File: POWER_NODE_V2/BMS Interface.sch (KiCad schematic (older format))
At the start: 11 parts

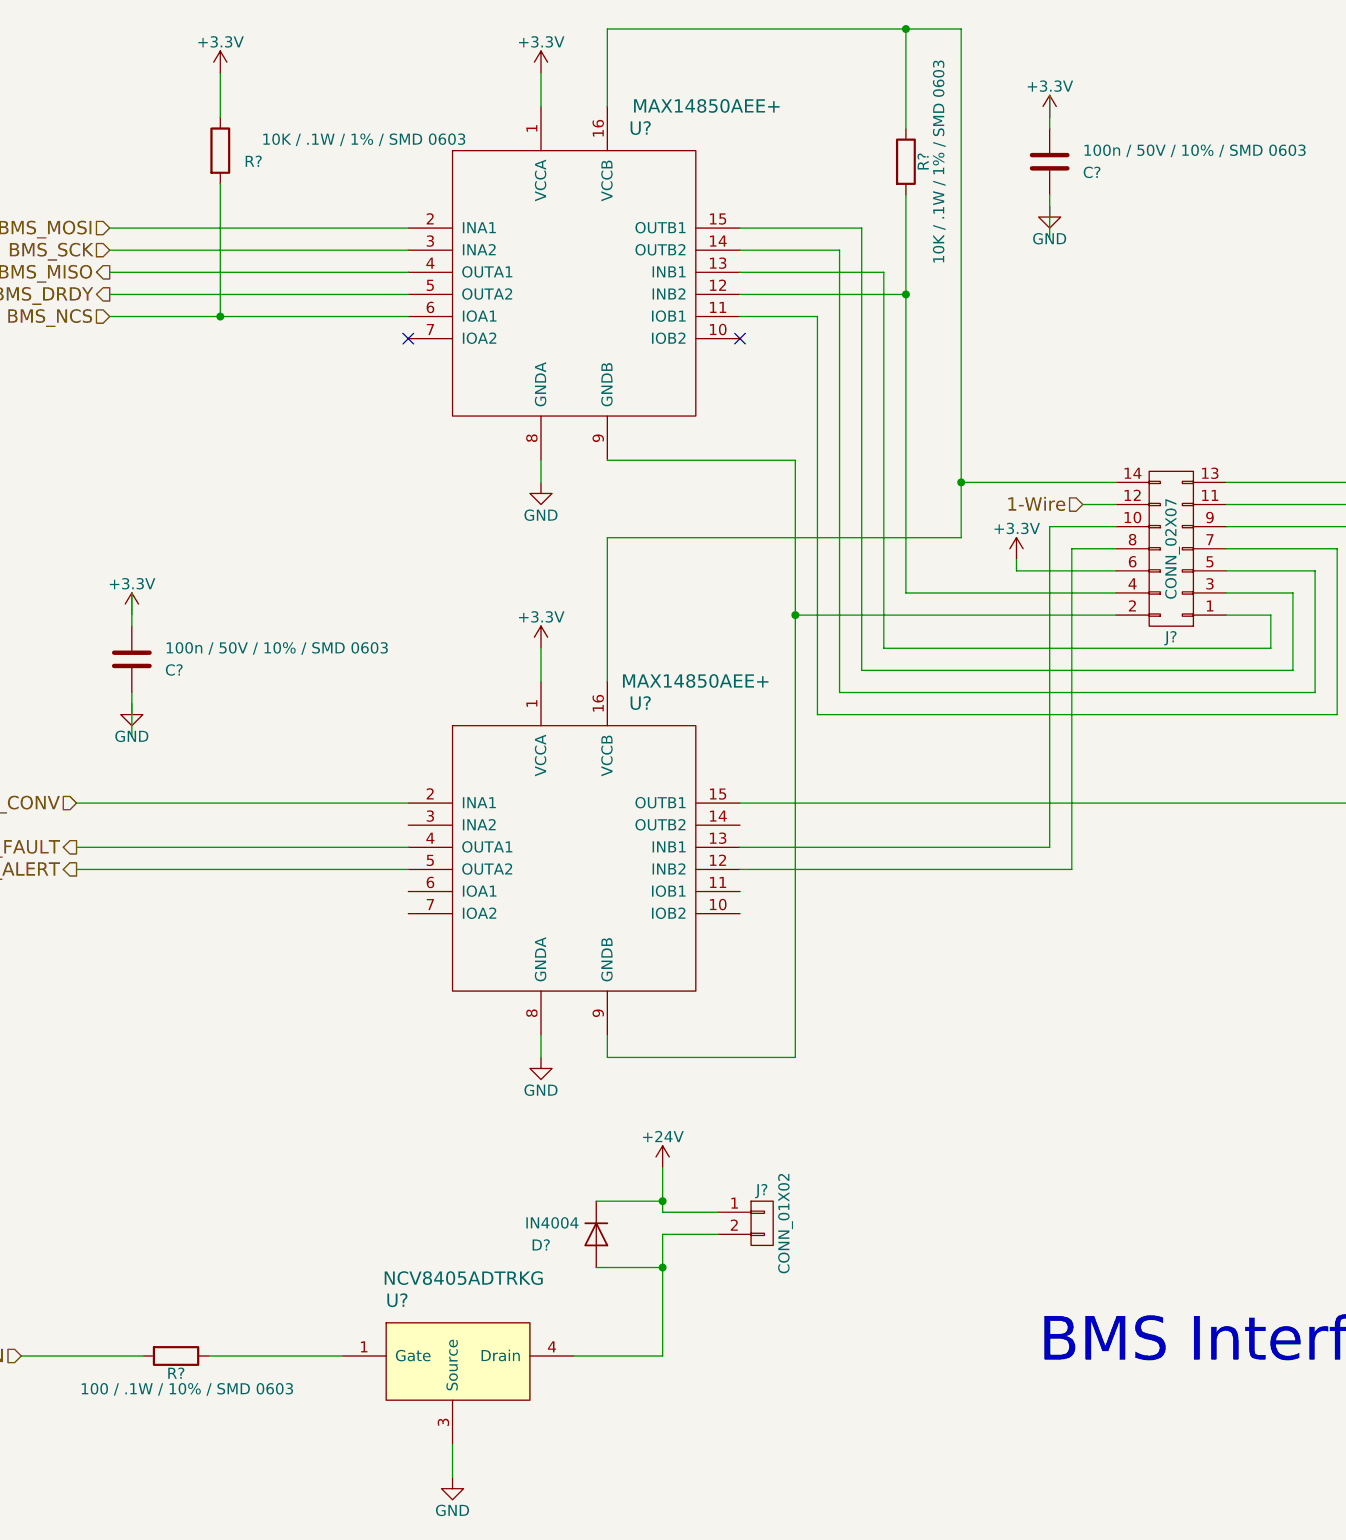
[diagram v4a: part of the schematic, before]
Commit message: made a lot of footprints, began PCB layout for power node v2
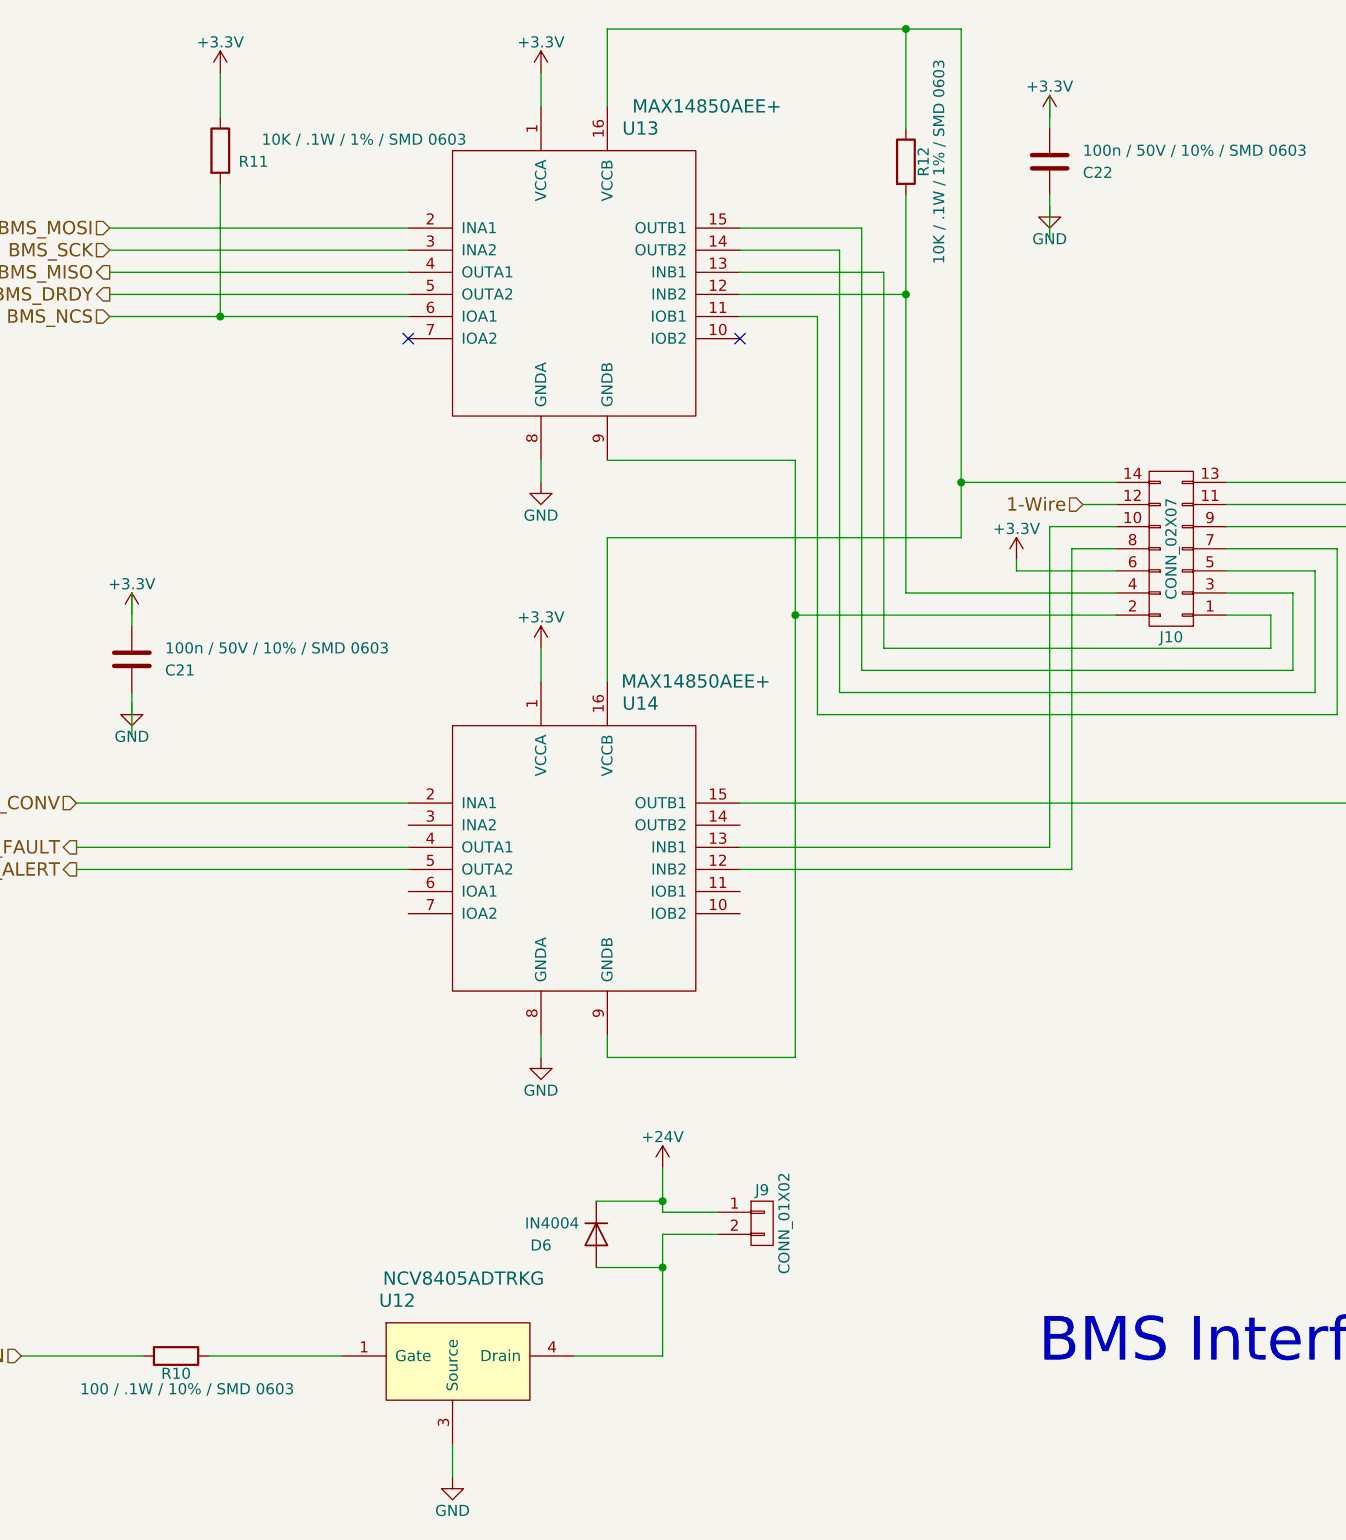
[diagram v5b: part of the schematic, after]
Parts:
- C21, C22: renamed from C?; footprint (none) -> Capacitors_SMD:C_0603
- D6: renamed from D?; footprint (none) -> Diodes_THT:D_DO-201_P15.24mm_Horizontal
- J10: renamed from J?; footprint (none) -> Pin_Headers:Pin_Header_Straight_2x07_Pitch2.54mm
- J9: renamed from J?; footprint (none) -> Pin_Headers:Pin_Header_Straight_1x02_Pitch2.54mm
- R10, R11, R12: renamed from R?; footprint (none) -> Resistors_SMD:R_0603
- U12: renamed from U?; footprint (none) -> TO_SOT_Packages_SMD:SOT-223
- U13, U14: renamed from U?; footprint (none) -> Housings_SSOP:QSOP-16_3.9x4.9mm_Pitch0.635mm
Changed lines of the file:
@@
 BMS_ALERT
 $Comp
-L MAX14850AEE+ U?
+L MAX14850AEE+ U13
 U 1 1 594CA282
 P 4300 2300
-F 0 "U?" H 4600 3000 60  0000 C CNN
+F 0 "U13" H 4600 3000 60  0000 C CNN
 F 1 "MAX14850AEE+" H 4900 3100 60  0000 C CNN
-F 2 "" H 4300 2300 60  0001 C CNN
+F 2 "Housings_SSOP:QSOP-16_3.9x4.9mm_Pitch0.635mm" H 4300 2300 60  0001 C CNN
 F 3 "" H 4300 2300 60  0001 C CNN
 	1    4300 2300
@@
 $EndComp
 $Comp
-L CONN_02X07 J?
+L CONN_02X07 J10
 U 1 1 594CA82A
 P 7000 3500
-F 0 "J?" H 7000 3900 50  0000 C CNN
+F 0 "J10" H 7000 3900 50  0000 C CNN
 F 1 "CONN_02X07" V 7000 3500 50  0000 C CNN
-F 2 "" H 7000 2300 50  0001 C CNN
+F 2 "Pin_Headers:Pin_Header_Straight_2x07_Pitch2.54mm" H 7000 2300 50  0001 C CNN
 F 3 "" H 7000 2300 50  0001 C CNN
 	1    7000 3500
@@
 $EndComp
 $Comp
-L GND #PWR?
+L GND #PWR097
 U 1 1 594CA92D
 P 8050 3350
-F 0 "#PWR?" H 8050 3100 50  0001 C CNN
+F 0 "#PWR097" H 8050 3100 50  0001 C CNN
 F 1 "GND" H 8050 3200 50  0000 C CNN
 F 2 "" H 8050 3350 50  0001 C CNN
@@
 $EndComp
 $Comp
-L +3.3V #PWR?
+L +3.3V #PWR098
 U 1 1 594CAB5E
 P 6300 3550
-F 0 "#PWR?" H 6300 3400 50  0001 C CNN
+F 0 "#PWR098" H 6300 3400 50  0001 C CNN
 F 1 "+3.3V" H 6300 3690 50  0000 C CNN
 F 2 "" H 6300 3550 50  0001 C CNN
@@
 1-Wire
 $Comp
-L R R?
+L R R11
 U 1 1 594CBA54
 P 2700 1700
-F 0 "R?" H 2850 1650 50  0000 C CNN
+F 0 "R11" H 2850 1650 50  0000 C CNN
 F 1 "10K / .1W / 1% / SMD 0603" H 3350 1750 50  0000 C CNN
-F 2 "" V 2630 1700 50  0001 C CNN
+F 2 "Resistors_SMD:R_0603" V 2630 1700 50  0001 C CNN
 F 3 "" H 2700 1700 50  0001 C CNN
 	1    2700 1700
@@
 $EndComp
 $Comp
-L +3.3V #PWR?
+L +3.3V #PWR099
 U 1 1 594CBADD
 P 4150 1350
-F 0 "#PWR?" H 4150 1200 50  0001 C CNN
+F 0 "#PWR099" H 4150 1200 50  0001 C CNN
 F 1 "+3.3V" H 4150 1490 50  0000 C CNN
 F 2 "" H 4150 1350 50  0001 C CNN
@@
 $EndComp
 $Comp
-L +3.3V #PWR?
+L +3.3V #PWR0100
 U 1 1 594CBAF4
 P 2700 1350
-F 0 "#PWR?" H 2700 1200 50  0001 C CNN
+F 0 "#PWR0100" H 2700 1200 50  0001 C CNN
 F 1 "+3.3V" H 2700 1490 50  0000 C CNN
 F 2 "" H 2700 1350 50  0001 C CNN
@@
 $EndComp
 $Comp
-L +3.3V #PWR?
+L +3.3V #PWR0101
 U 1 1 594CBB5B
 P 4150 3950
-F 0 "#PWR?" H 4150 3800 50  0001 C CNN
+F 0 "#PWR0101" H 4150 3800 50  0001 C CNN
 F 1 "+3.3V" H 4150 4090 50  0000 C CNN
 F 2 "" H 4150 3950 50  0001 C CNN
@@
 $EndComp
 $Comp
-L R R?
+L R R12
 U 1 1 594CBB70
 P 5800 1750
-F 0 "R?" V 5880 1750 50  0000 C CNN
+F 0 "R12" V 5880 1750 50  0000 C CNN
 F 1 "10K / .1W / 1% / SMD 0603" V 5950 1750 50  0000 C CNN
-F 2 "" V 5730 1750 50  0001 C CNN
+F 2 "Resistors_SMD:R_0603" V 5730 1750 50  0001 C CNN
 F 3 "" H 5800 1750 50  0001 C CNN
 	1    5800 1750
@@
 $EndComp
 $Comp
-L GND #PWR?
+L GND #PWR0102
 U 1 1 594CBF3C
 P 4150 3200
-F 0 "#PWR?" H 4150 2950 50  0001 C CNN
+F 0 "#PWR0102" H 4150 2950 50  0001 C CNN
 F 1 "GND" H 4150 3050 50  0000 C CNN
 F 2 "" H 4150 3200 50  0001 C CNN
@@
 $EndComp
 $Comp
-L GND #PWR?
+L GND #PWR0103
 U 1 1 594CBFA2
 P 4150 5800
-F 0 "#PWR?" H 4150 5550 50  0001 C CNN
+F 0 "#PWR0103" H 4150 5550 50  0001 C CNN
 F 1 "GND" H 4150 5650 50  0000 C CNN
 F 2 "" H 4150 5800 50  0001 C CNN
@@
 NoConn ~ 5050 2550
 $Comp
-L CONN_01X02 J?
+L CONN_01X02 J9
 U 1 1 594DEEA6
 P 5150 6550
-F 0 "J?" H 5150 6700 50  0000 C CNN
+F 0 "J9" H 5150 6700 50  0000 C CNN
 F 1 "CONN_01X02" V 5250 6550 50  0000 C CNN
-F 2 "" H 5150 6550 50  0001 C CNN
+F 2 "Pin_Headers:Pin_Header_Straight_1x02_Pitch2.54mm" H 5150 6550 50  0001 C CNN
 F 3 "" H 5150 6550 50  0001 C CNN
 	1    5150 6550
@@
 $EndComp
 $Comp
-L R R?
+L R R10
 U 1 1 594DF1C9
 P 2500 7150
-F 0 "R?" V 2580 7150 50  0000 C CNN
+F 0 "R10" V 2580 7150 50  0000 C CNN
 F 1 "100 / .1W / 10% / SMD 0603" V 2650 7200 50  0000 C CNN
-F 2 "" V 2430 7150 50  0001 C CNN
+F 2 "Resistors_SMD:R_0603" V 2430 7150 50  0001 C CNN
 F 3 "" H 2500 7150 50  0001 C CNN
 	1    2500 7150
@@
 $EndComp
 $Comp
-L GND #PWR?
+L GND #PWR0104
 U 1 1 594DF3E0
 P 3750 7700
-F 0 "#PWR?" H 3750 7450 50  0001 C CNN
+F 0 "#PWR0104" H 3750 7450 50  0001 C CNN
 F 1 "GND" H 3750 7550 50  0000 C CNN
 F 2 "" H 3750 7700 50  0001 C CNN
@@
 $EndComp
 $Comp
-L +24V #PWR?
+L +24V #PWR0105
 U 1 1 594DF525
 P 4700 6300
-F 0 "#PWR?" H 4700 6150 50  0001 C CNN
+F 0 "#PWR0105" H 4700 6150 50  0001 C CNN
 F 1 "+24V" H 4700 6440 50  0000 C CNN
 F 2 "" H 4700 6300 50  0001 C CNN
@@
 $EndComp
 $Comp
-L C C?
+L C C22
 U 1 1 59514BAA
 P 6450 1750
-F 0 "C?" H 6600 1700 50  0000 L CNN
+F 0 "C22" H 6600 1700 50  0000 L CNN
 F 1 "100n / 50V / 10% / SMD 0603" H 6600 1800 50  0000 L CNN
-F 2 "" H 6488 1600 50  0001 C CNN
+F 2 "Capacitors_SMD:C_0603" H 6488 1600 50  0001 C CNN
 F 3 "" H 6450 1750 50  0001 C CNN
 	1    6450 1750
@@
 $EndComp
 $Comp
-L +3.3V #PWR?
+L +3.3V #PWR0106
 U 1 1 59514C06
 P 6450 1550
-F 0 "#PWR?" H 6450 1400 50  0001 C CNN
+F 0 "#PWR0106" H 6450 1400 50  0001 C CNN
 F 1 "+3.3V" H 6450 1690 50  0000 C CNN
 F 2 "" H 6450 1550 50  0001 C CNN
@@
 $EndComp
 $Comp
-L GND #PWR?
+L GND #PWR0107
 U 1 1 59514D0B
 P 6450 1950
-F 0 "#PWR?" H 6450 1700 50  0001 C CNN
+F 0 "#PWR0107" H 6450 1700 50  0001 C CNN
 F 1 "GND" H 6450 1800 50  0000 C CNN
 F 2 "" H 6450 1950 50  0001 C CNN
@@
 $EndComp
 $Comp
-L C C?
+L C C21
 U 1 1 59515426
 P 2300 4000
-F 0 "C?" H 2450 3950 50  0000 L CNN
+F 0 "C21" H 2450 3950 50  0000 L CNN
 F 1 "100n / 50V / 10% / SMD 0603" H 2450 4050 50  0000 L CNN
-F 2 "" H 2338 3850 50  0001 C CNN
+F 2 "Capacitors_SMD:C_0603" H 2338 3850 50  0001 C CNN
 F 3 "" H 2300 4000 50  0001 C CNN
 	1    2300 4000
@@
 $EndComp
 $Comp
-L +3.3V #PWR?
+L +3.3V #PWR0108
 U 1 1 5951542C
 P 2300 3800
-F 0 "#PWR?" H 2300 3650 50  0001 C CNN
+F 0 "#PWR0108" H 2300 3650 50  0001 C CNN
 F 1 "+3.3V" H 2300 3940 50  0000 C CNN
 F 2 "" H 2300 3800 50  0001 C CNN
@@
 $EndComp
 $Comp
-L GND #PWR?
+L GND #PWR0109
 U 1 1 59515432
 P 2300 4200
-F 0 "#PWR?" H 2300 3950 50  0001 C CNN
+F 0 "#PWR0109" H 2300 3950 50  0001 C CNN
 F 1 "GND" H 2300 4050 50  0000 C CNN
 F 2 "" H 2300 4200 50  0001 C CNN
@@
 $EndComp
 $Comp
-L MAX14850AEE+ U?
+L MAX14850AEE+ U14
 U 1 1 595156F6
 P 4300 4900
-F 0 "U?" H 4600 5600 60  0000 C CNN
+F 0 "U14" H 4600 5600 60  0000 C CNN
 F 1 "MAX14850AEE+" H 4850 5700 60  0000 C CNN
-F 2 "" H 4300 4900 60  0001 C CNN
+F 2 "Housings_SSOP:QSOP-16_3.9x4.9mm_Pitch0.635mm" H 4300 4900 60  0001 C CNN
 F 3 "" H 4300 4900 60  0001 C CNN
 	1    4300 4900
@@
 $EndComp
 $Comp
-L D D?
+L D D6
 U 1 1 595161C1
 P 4400 6600
-F 0 "D?" V 4450 6350 50  0000 C CNN
+F 0 "D6" V 4450 6350 50  0000 C CNN
 F 1 "IN4004" V 4350 6400 50  0000 C CNN
-F 2 "" H 4400 6600 50  0001 C CNN
+F 2 "Diodes_THT:D_DO-201_P15.24mm_Horizontal" H 4400 6600 50  0001 C CNN
 F 3 "" H 4400 6600 50  0001 C CNN
 	1    4400 6600
@@
 Connection ~ 4700 6750
 $Comp
-L NCV8405ADTRKG U?
+L NCV8405ADTRKG U12
 U 1 1 59516F9D
 P 3750 7200
-F 0 "U?" H 3500 7500 60  0000 C CNN
+F 0 "U12" H 3500 7500 60  0000 C CNN
 F 1 "NCV8405ADTRKG" H 3800 7600 60  0000 C CNN
-F 2 "" H 3750 7100 60  0001 C CNN
+F 2 "TO_SOT_Packages_SMD:SOT-223" H 3750 7100 60  0001 C CNN
 F 3 "" H 3750 7100 60  0001 C CNN
 	1    3750 7200
